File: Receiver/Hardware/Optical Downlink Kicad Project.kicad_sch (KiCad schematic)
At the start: 20 parts, among them J1 Conn_01x20_Socket, J2 Conn_01x20_Socket, U1 OPA657U, U2 TLE2426-EP_D_8, U3 OPA657U, U4 ADS8691IPWR, U5 MEVS0509SC, U6 HT7580-2

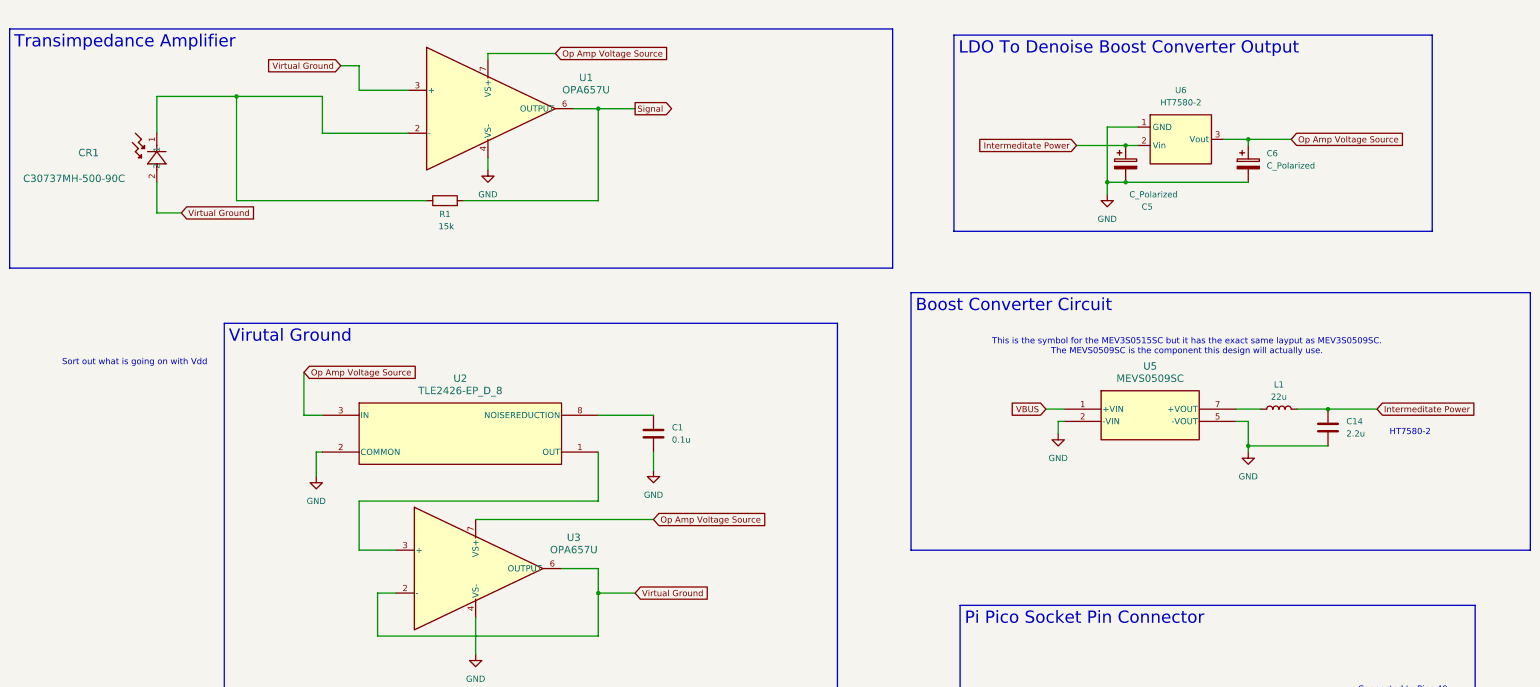
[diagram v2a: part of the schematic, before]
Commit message: Cleaned Up Some of The Power Net Names
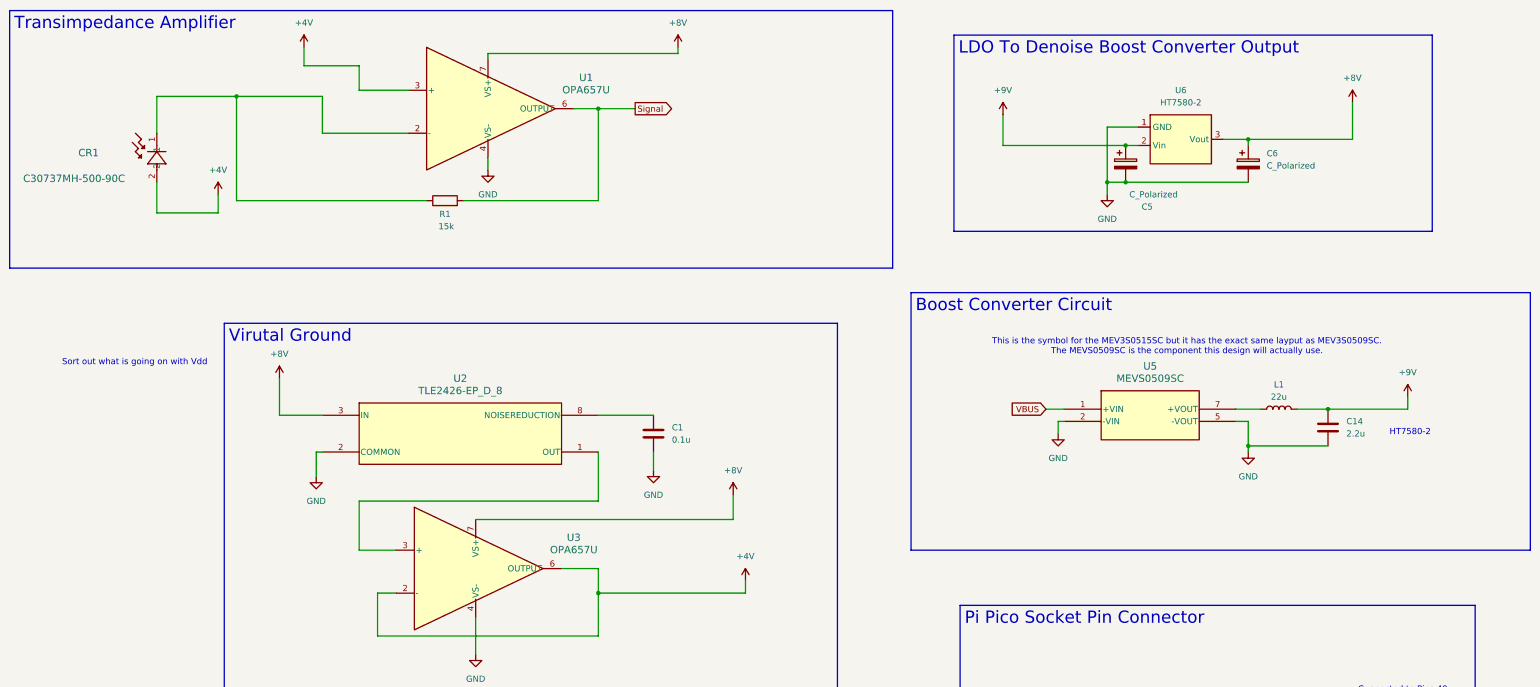
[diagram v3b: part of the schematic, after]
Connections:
- net Intermeditate Power renamed +9V
- net Op Amp Voltage Source renamed +8V
- net Virtual Ground renamed +4V

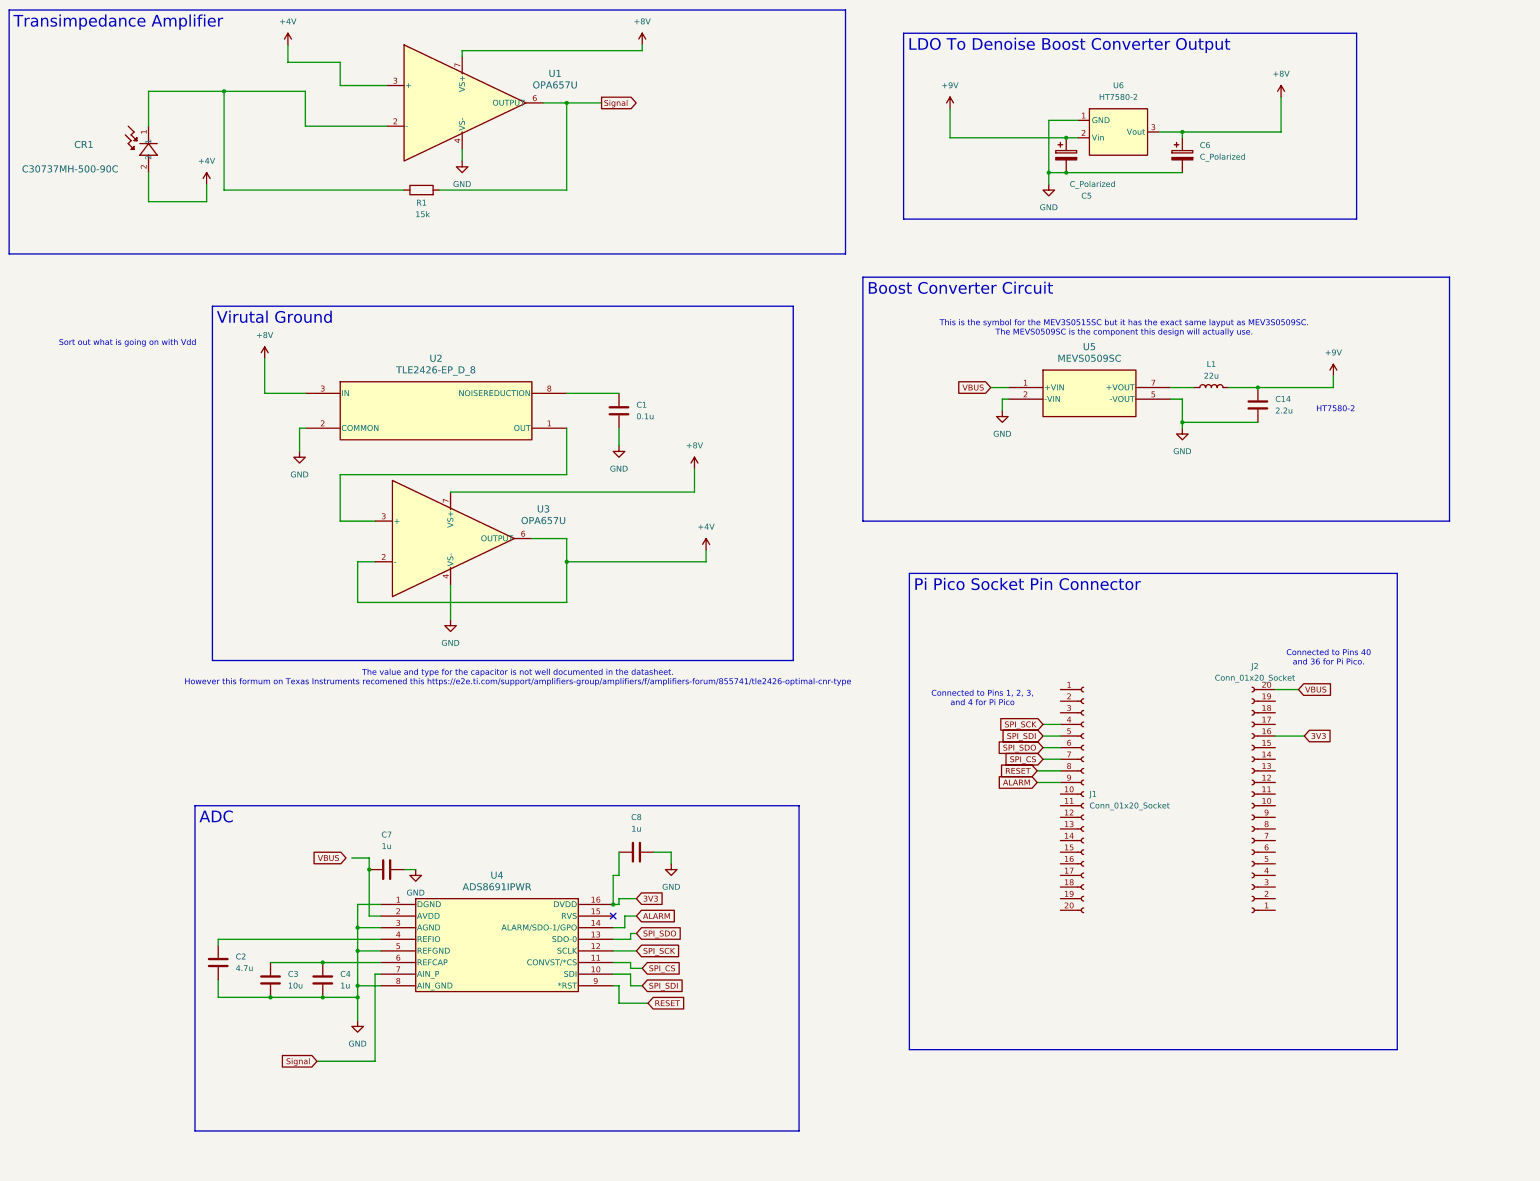
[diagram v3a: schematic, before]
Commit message: Cleaned up Schematic a bit
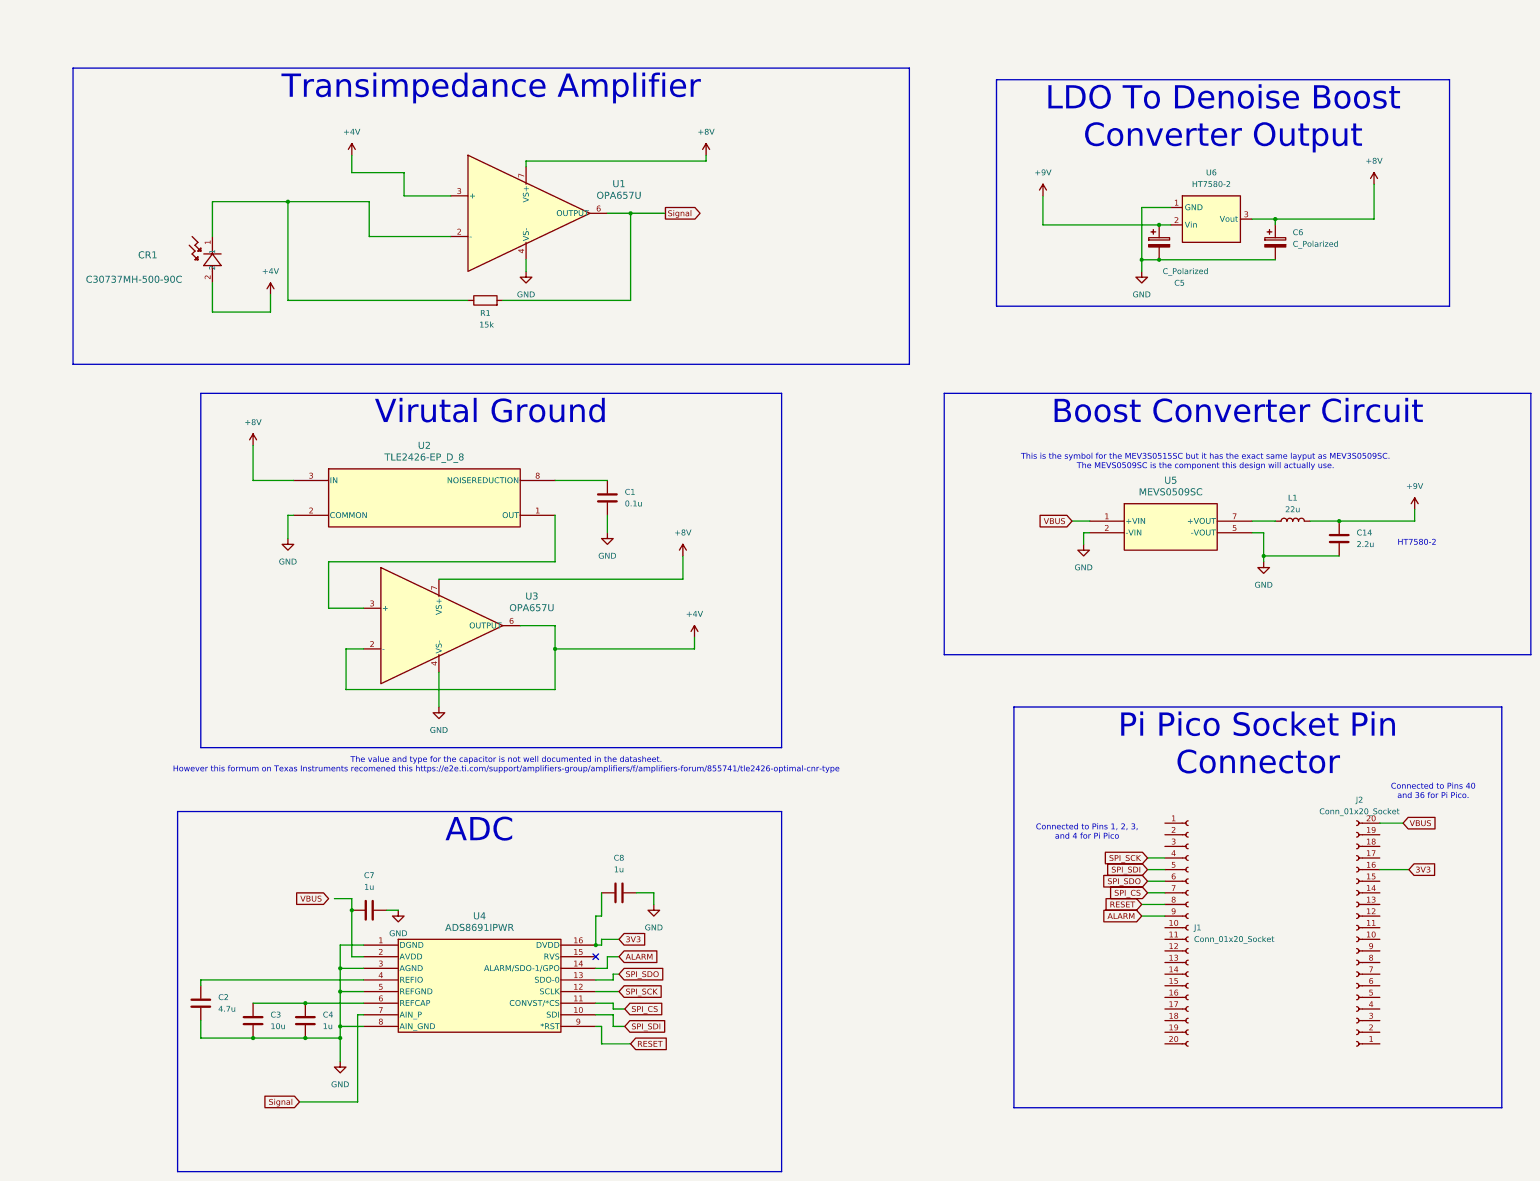
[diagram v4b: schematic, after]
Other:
- note removed: "Sort out what is going on with Vdd"
- moved on the sheet: C1, C14, C2, C3, C4, C5, C6, C7, C8, CR1, J1, J2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

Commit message: Simulation added for proper redesign of reciever
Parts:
- C5, C6: value C_Polarized -> 10u
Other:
- moved on the sheet: C1, C14, C2, C3, C4, C5, C6, C7, C8, CR1, J1, J2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
